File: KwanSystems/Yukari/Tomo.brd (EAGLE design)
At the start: 35.6 x 35.6 mm, 22 parts, among them U1 NCP1402, U2 741034

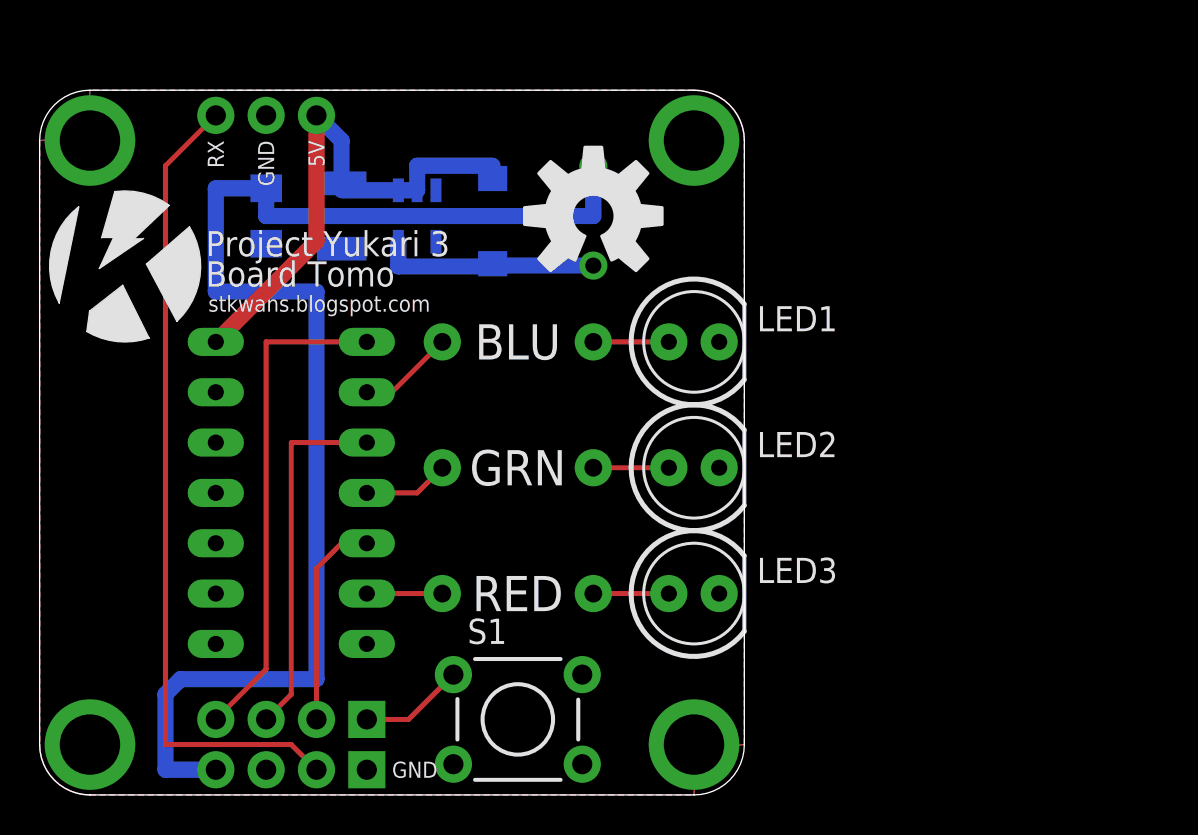
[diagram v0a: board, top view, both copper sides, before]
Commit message: Added LegoClassicSpace.svg after checking local copy. We'll see how the pull works
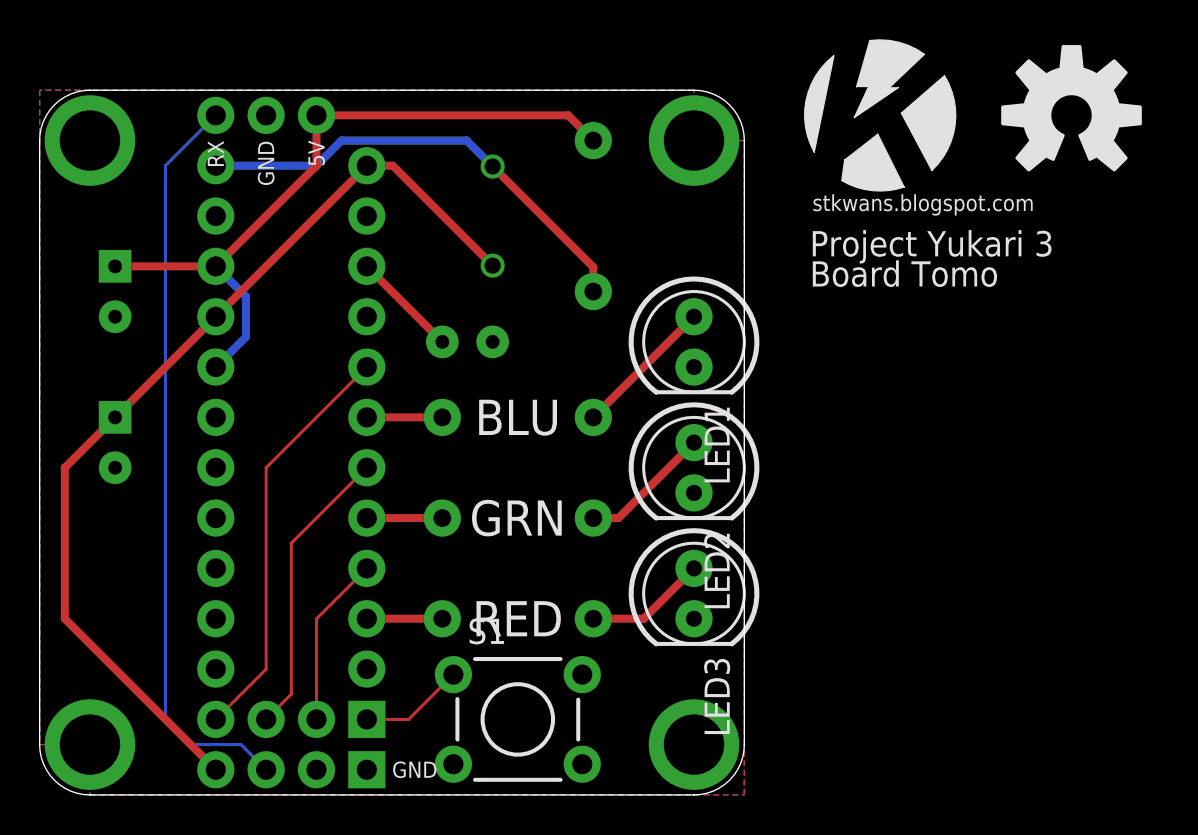
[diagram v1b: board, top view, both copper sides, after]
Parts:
- removed U1: NCP1402, SparkFun:SOT23-5
- added C3: 100uF, SparkFun-Capacitors:CPOL-RADIAL-100UF-25V
- added U$2: MAX756, KwanSystems:DIL-8
- C1: value 10uF -> 150uF; device SparkFun:EIA3216 -> SparkFun-Capacitors:CPOL-RADIAL-100UF-25V
- C2: value 68uF -> 100nF; device SparkFun:EIA3528 -> SparkFun-Capacitors:CAP-PTH-SMALL
- D1: value MBRA140 -> 1N5817; device SparkFun:SMA-DIODE -> SparkFun-DiscreteSemi:DIODE-1N4148
- L1: value 47uH -> 22uH
- moved U$7 38.9 mm to (42.4, 34.3)
- moved U$1 24.7 mm to (52.1, 34.3)
- moved C1 13.7 mm to (3.81, 17.8)
- moved C2 8.13 mm to (20.3, 22.9), turned to 180 degrees
- moved D1 5.09 mm to (27.9, 29.2)
- moved L1 5.08 mm to (22.9, 29.2), turned to 0 degrees
- moved R1 3.81 mm to (24.1, 19.1)
- moved R2 2.54 mm to (24.1, 14.0)
- moved R3 1.27 mm to (24.1, 8.89)
- moved U2 1.27 mm to (12.7, 14.0)
- turned LED1 to 270 degrees
- turned LED2 to 270 degrees
- turned LED3 to 270 degrees
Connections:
- new net N$8: C2.1, U$2.3
- net 3V3: now also C1.1, U$2.1, U$2.5; no longer C1.A
- net 5V: now also C3.1, U$2.6; no longer C2.A, U1.1, U1.2
- net GND: now also C1.2, C2.2, C3.2, U$2.2, U$2.7, U2.11, U2.13, U2.9; no longer C1.C, C2.C, U1.4
- net N$3: now also U$2.8; no longer U1.5
- net RX0: now also JP3.2; no longer JP3.3
- net TX0: now also JP3.3; no longer JP3.2
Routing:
- net 3V3: track 67.1 -> 48.4 mm
- net N$3: track 11.3 -> 23.5 mm
- net 5V: track 27.3 -> 35.6 mm
- net N$8: track 0.00 -> 5.39 mm
- net BLUE: track 25.2 -> 20.9 mm
- net GREEN: track 18.3 -> 14.8 mm
- net N$1: track 3.81 -> 7.18 mm
- net TX0: track 40.9 -> 37.7 mm
- net N$2: track 3.81 -> 6.66 mm
- net N$4: track 3.81 -> 6.13 mm
- net RED: track 10.7 -> 8.67 mm
- net N$5: track 4.86 -> 3.81 mm
- net N$6: track 4.34 -> 3.81 mm
